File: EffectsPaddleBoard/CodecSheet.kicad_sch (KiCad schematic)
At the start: 22 parts, among them U3 TLV320AIC3100

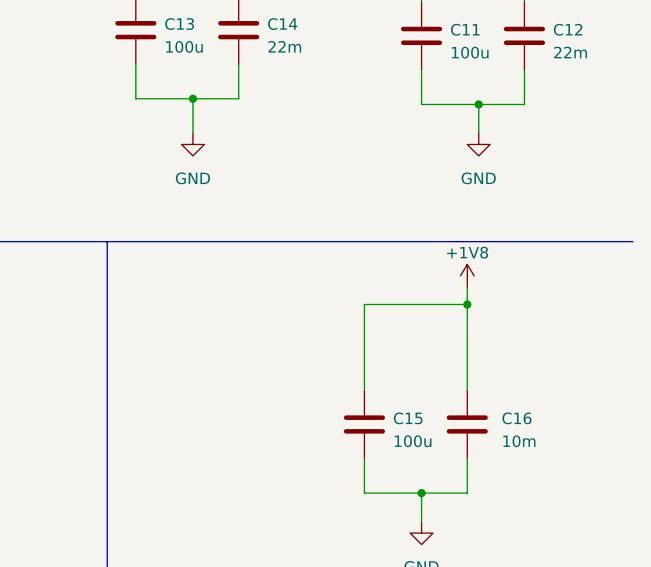
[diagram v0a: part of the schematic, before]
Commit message: Added 3d models
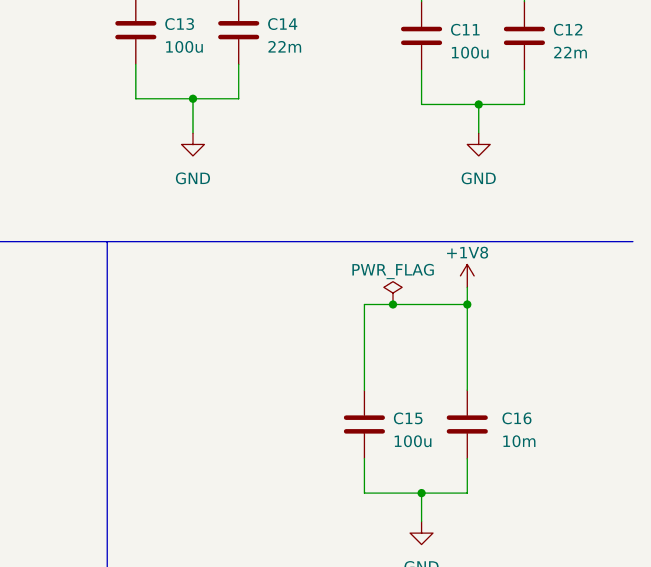
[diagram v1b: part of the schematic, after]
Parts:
- U3: Distributer Link (none) -> https://www.mouser.ch/ProductDetail/Texas-Instruments/TLV32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; Manufacturer (none) -> Texas Instruments; Manufacturer Part Number (none) -> TLV320AIC3100IRHBR
